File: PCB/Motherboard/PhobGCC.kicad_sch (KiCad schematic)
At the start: 57 parts, among them J1 Conn_01x06_Female, J2 Conn_01x04_Female, J3 Conn_01x01_Male, J5 Conn_01x02_Male, Q1 SSM3K56FS,LF, SW1 A, SW10 Dup, SW11 Dright, SW12 Ddown, SW2 B, SW3 X, SW4 Y, SW5 Start, SW6 L, SW7 R, SW8 1825027-5, SW9 Dleft, U1 Teensy4.0, U2 2x DRV5053CAQLPGM Hall Effect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, U3 BPR-105, U4 BPR-105

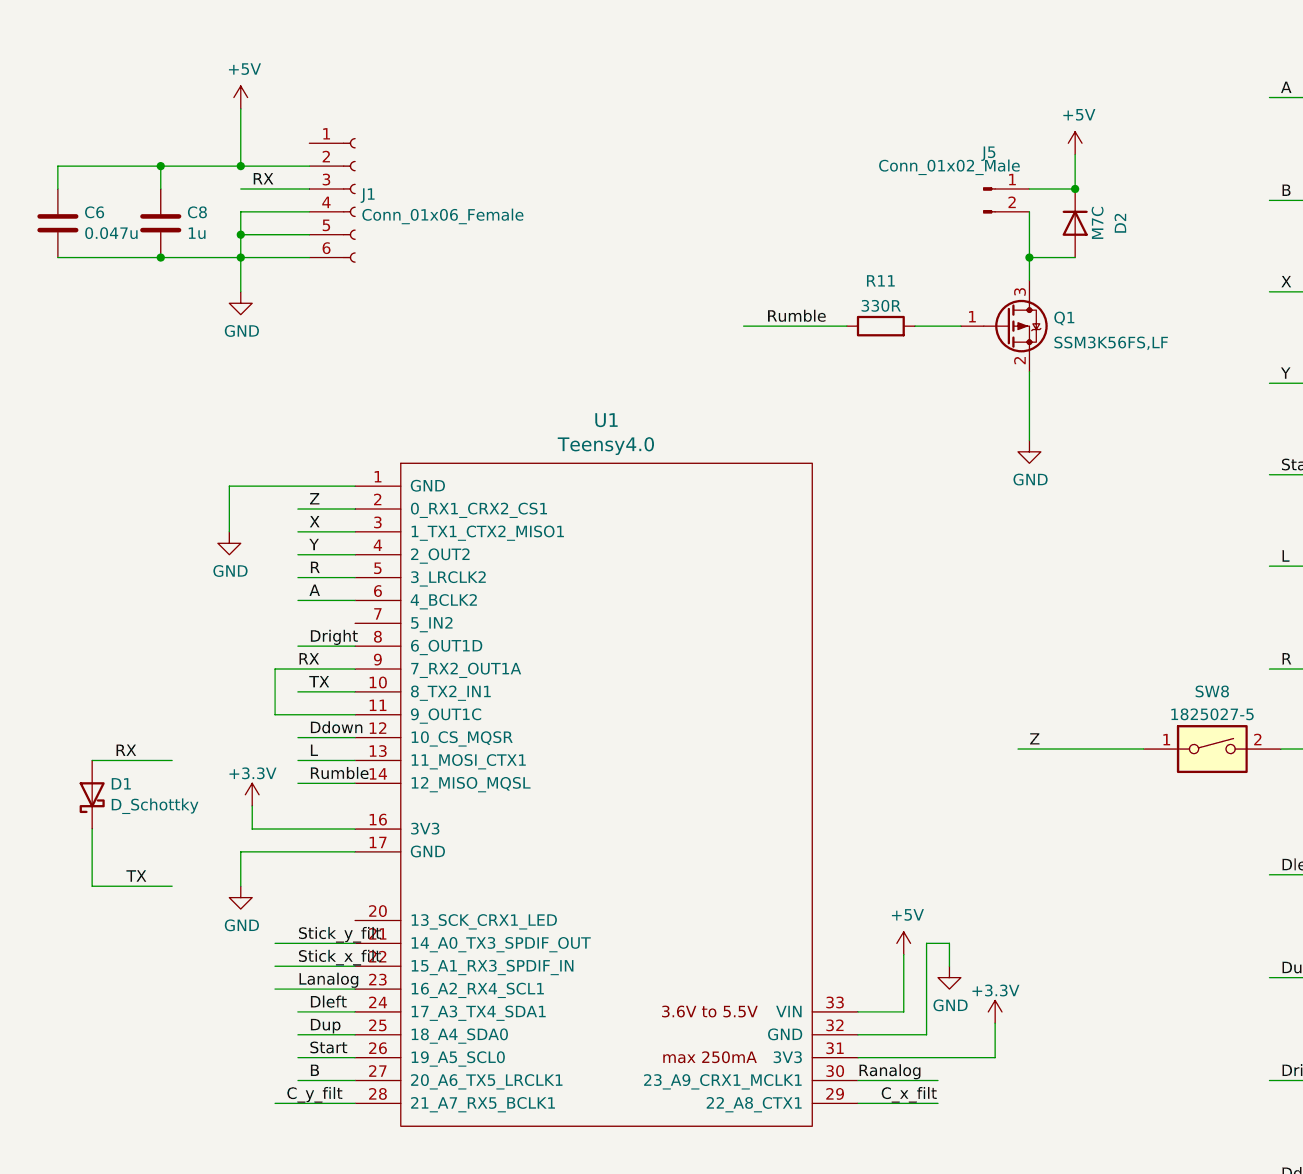
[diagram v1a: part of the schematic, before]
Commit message: Tidied up some things in the PCB, redid the ABXY contacts from an earlier file version, preview now works on jlcPCB
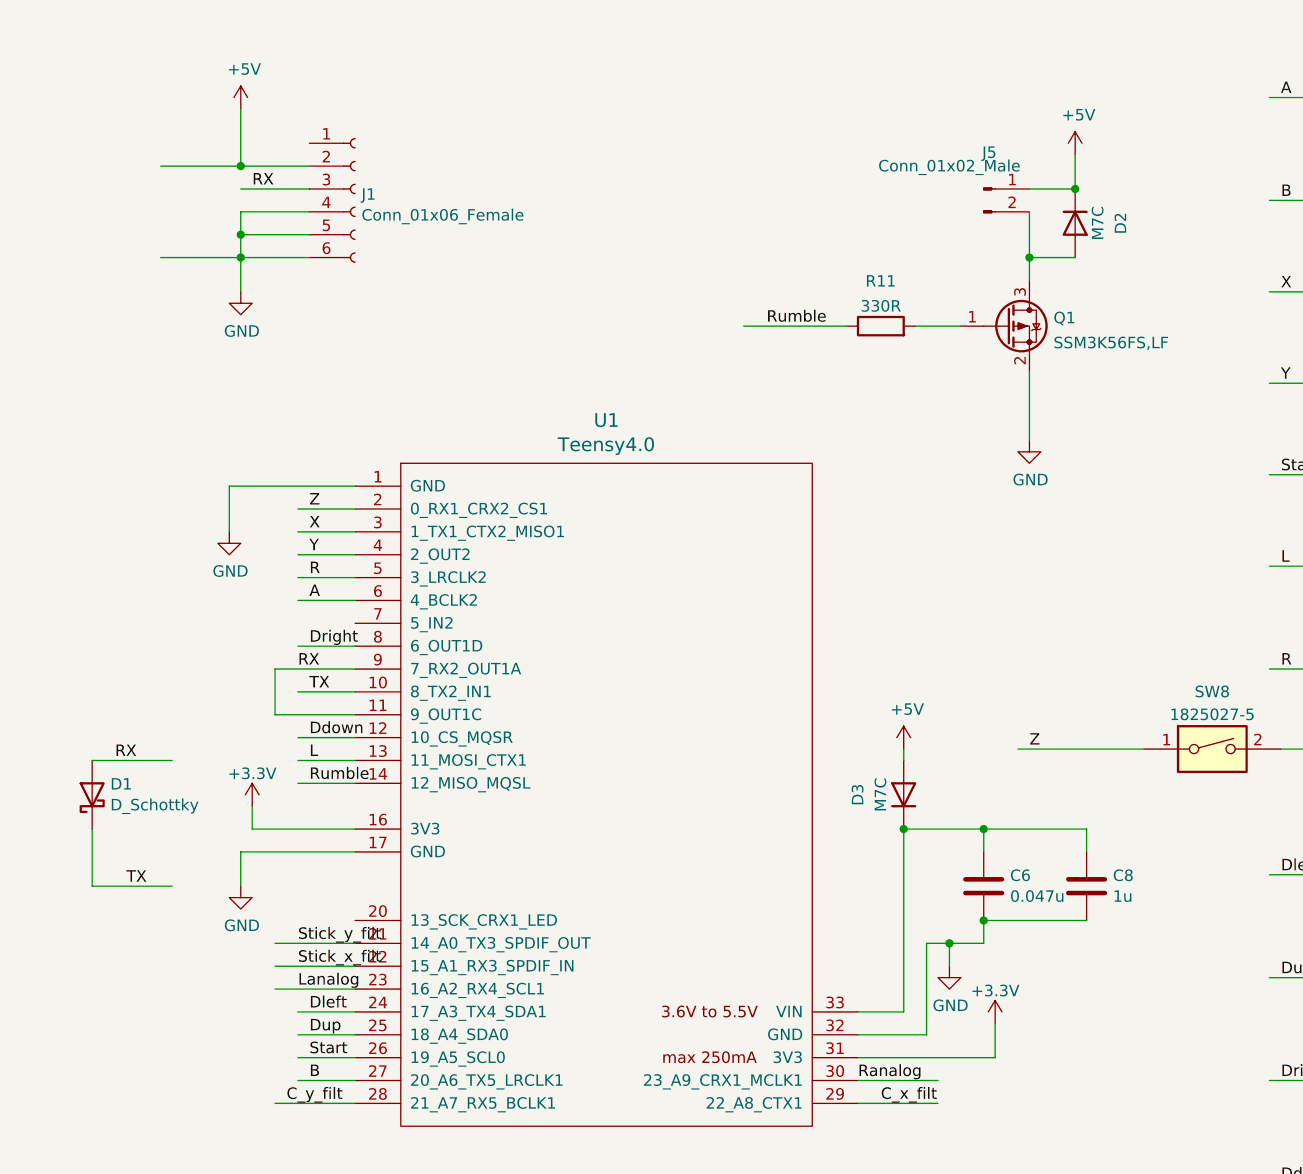
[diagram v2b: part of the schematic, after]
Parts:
- added D3: M7C, Diode_SMD:D_SOD-123F, symbol Device:D
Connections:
- net +5V: now also D3.2 (A); no longer C6.1, C8.1, U1.33 (VIN)
- new net: C6.1, C8.1, D3.1 (K), U1.33 (VIN)
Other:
- moved on the sheet: C6, C8
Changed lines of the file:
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@@
   (junction (at 133.35 180.34) (diameter 0) (color 0 0 0 0)
   )
+  (junction (at 119.38 116.84) (diameter 0) (color 0 0 0 0)
+  )
   (junction (at 177.8 44.45) (diameter 0) (color 0 0 0 0)
   )
@@
   (junction (at 177.8 132.08) (diameter 0) (color 0 0 0 0)
   )
+  (junction (at 123.19 104.14) (diameter 0) (color 0 0 0 0)
+  )
   (junction (at 90.17 180.34) (diameter 0) (color 0 0 0 0)
   )
@@
   (junction (at 80.01 180.34) (diameter 0) (color 0 0 0 0)
   )
+  (junction (at 114.3 104.14) (diameter 0) (color 0 0 0 0)
+  )
   (junction (at 228.6 31.75) (diameter 0) (color 0 0 0 0)
   )
@@
   (junction (at 76.2 168.91) (diameter 0) (color 0 0 0 0)
   )
-  (junction (at 31.75 40.64) (diameter 0) (color 0 0 0 0)
-  )
   (junction (at 99.06 180.34) (diameter 0) (color 0 0 0 0)
   )
@@
   (junction (at 40.64 40.64) (diameter 0) (color 0 0 0 0)
   )
+  (junction (at 123.19 114.3) (diameter 0) (color 0 0 0 0)
+  )
   (junction (at 226.06 59.69) (diameter 0) (color 0 0 0 0)
   )
@@
   (junction (at 76.2 180.34) (diameter 0) (color 0 0 0 0)
   )
-  (junction (at 31.75 30.48) (diameter 0) (color 0 0 0 0)
-  )
   (junction (at 209.55 143.51) (diameter 0) (color 0 0 0 0)
   )
@@
     (stroke (width 0) (type default) (color 0 0 0 0))
   )
+  (wire (pts (xy 123.19 114.3) (xy 123.19 116.84))
+    (stroke (width 0) (type default) (color 0 0 0 0))
+  )
   (wire (pts (xy 241.3 21.59) (xy 226.06 21.59))
     (stroke (width 0) (type default) (color 0 0 0 0))
   )
+  (wire (pts (xy 114.3 104.14) (xy 114.3 124.46))
+    (stroke (width 0) (type default) (color 0 0 0 0))
+  )
   (wire (pts (xy 40.64 180.34) (xy 60.96 180.34))
     (stroke (width 0) (type default) (color 0 0 0 0))
@@
     (stroke (width 0) (type default) (color 0 0 0 0))
   )
+  (wire (pts (xy 114.3 95.25) (xy 114.3 96.52))
+    (stroke (width 0) (type default) (color 0 0 0 0))
+  )
   (wire (pts (xy 53.34 86.36) (xy 44.45 86.36))
     (stroke (width 0) (type default) (color 0 0 0 0))
@@
     (stroke (width 0) (type default) (color 0 0 0 0))
   )
-  (wire (pts (xy 31.75 33.02) (xy 31.75 30.48))
-    (stroke (width 0) (type default) (color 0 0 0 0))
-  )
-  (wire (pts (xy 20.32 30.48) (xy 31.75 30.48))
+  (wire (pts (xy 134.62 106.68) (xy 134.62 104.14))
+    (stroke (width 0) (type default) (color 0 0 0 0))
+  )
+  (wire (pts (xy 114.3 104.14) (xy 123.19 104.14))
+    (stroke (width 0) (type default) (color 0 0 0 0))
+  )
+  (wire (pts (xy 123.19 104.14) (xy 134.62 104.14))
     (stroke (width 0) (type default) (color 0 0 0 0))
   )
@@
     (stroke (width 0) (type default) (color 0 0 0 0))
   )
-  (wire (pts (xy 20.32 30.48) (xy 20.32 33.02))
+  (wire (pts (xy 123.19 104.14) (xy 123.19 106.68))
     (stroke (width 0) (type default) (color 0 0 0 0))
   )
@@
     (stroke (width 0) (type default) (color 0 0 0 0))
   )
+  (wire (pts (xy 123.19 116.84) (xy 119.38 116.84))
+    (stroke (width 0) (type default) (color 0 0 0 0))
+  )
   (wire (pts (xy 163.83 74.93) (xy 154.94 74.93))
     (stroke (width 0) (type default) (color 0 0 0 0))
@@
     (stroke (width 0) (type default) (color 0 0 0 0))
   )
-  (wire (pts (xy 114.3 124.46) (xy 114.3 118.11))
-    (stroke (width 0) (type default) (color 0 0 0 0))
-  )
   (wire (pts (xy 173.99 143.51) (xy 177.8 143.51))
     (stroke (width 0) (type default) (color 0 0 0 0))
@@
     (stroke (width 0) (type default) (color 0 0 0 0))
   )
-  (wire (pts (xy 20.32 40.64) (xy 31.75 40.64))
+  (wire (pts (xy 123.19 114.3) (xy 134.62 114.3))
     (stroke (width 0) (type default) (color 0 0 0 0))
   )
@@
     (pin "1")
   )
-  (symbol (lib_id "Device:C") (at 31.75 36.83 0) (unit 1)
-    (in_bom yes) (on_board yes)
-    (property "Reference" "C8" (id 0) (at 34.671 35.6616 0)
-      (effects (font (size 1.27 1.27)) (justify left))
-    )
-    (property "Value" "1u" (id 1) (at 34.671 37.973 0)
-      (effects (font (size 1.27 1.27)) (justify left))
-    )
-    (property "Footprint" "Capacitors_SMD:C_0603_HandSoldering" (id 2) (at 32.7152 40.64 0)
-      (effects (font (size 1.27 1.27)) hide)
-    )
-    (property "Datasheet" "~" (id 3) (at 31.75 36.83 0)
-      (effects (font (size 1.27 1.27)) hide)
-    )
-    (property "LCSC" "C15849" (id 4) (at 31.75 36.83 0)
-      (effects (font (size 1.27 1.27)) hide)
-    )
-    (property "MPN" "CL10A105KB8NNNC" (id 5) (at 31.75 36.83 0)
-      (effects (font (size 1.27 1.27)) hide)
-    )
-    (property "Manufacturer" "Samsung Electro-Mechanics" (id 6) (at 31.75 36.83 0)
-      (effects (font (size 1.27 1.27)) hide)
-    )
-    (pin "1")
-    (pin "2")
-  )
-  (symbol (lib_id "power:+5V") (at 114.3 118.11 0) (unit 1)
-    (in_bom yes) (on_board yes)
-    (property "Reference" "#PWR0118" (id 0) (at 114.3 121.92 0)
-      (effects (font (size 1.27 1.27)) hide)
-    )
-    (property "Value" "+5V" (id 1) (at 114.681 113.7158 0))
-    (property "Footprint" "" (id 2) (at 114.3 118.11 0)
-      (effects (font (size 1.27 1.27)) hide)
-    )
-    (property "Datasheet" "" (id 3) (at 114.3 118.11 0)
+  (symbol (lib_id "Device:C") (at 134.62 110.49 0) (unit 1)
+    (in_bom yes) (on_board yes)
+    (property "Reference" "C8" (id 0) (at 137.541 109.3216 0)
+      (effects (font (size 1.27 1.27)) (justify left))
+    )
+    (property "Value" "1u" (id 1) (at 137.541 111.633 0)
+      (effects (font (size 1.27 1.27)) (justify left))
+    )
+    (property "Footprint" "Capacitors_SMD:C_0603_HandSoldering" (id 2) (at 135.5852 114.3 0)
+      (effects (font (size 1.27 1.27)) hide)
+    )
+    (property "Datasheet" "~" (id 3) (at 134.62 110.49 0)
+      (effects (font (size 1.27 1.27)) hide)
+    )
+    (property "LCSC" "C15849" (id 4) (at 134.62 110.49 0)
+      (effects (font (size 1.27 1.27)) hide)
+    )
+    (property "MPN" "CL10A105KB8NNNC" (id 5) (at 134.62 110.49 0)
+      (effects (font (size 1.27 1.27)) hide)
+    )
+    (property "Manufacturer" "Samsung Electro-Mechanics" (id 6) (at 134.62 110.49 0)
+      (effects (font (size 1.27 1.27)) hide)
+    )
+    (pin "1")
+    (pin "2")
+  )
+  (symbol (lib_id "power:+5V") (at 114.3 95.25 0) (unit 1)
+    (in_bom yes) (on_board yes)
+    (property "Reference" "#PWR0118" (id 0) (at 114.3 99.06 0)
+      (effects (font (size 1.27 1.27)) hide)
+    )
+    (property "Value" "+5V" (id 1) (at 114.681 90.8558 0))
+    (property "Footprint" "" (id 2) (at 114.3 95.25 0)
+      (effects (font (size 1.27 1.27)) hide)
+    )
+    (property "Datasheet" "" (id 3) (at 114.3 95.25 0)
       (effects (font (size 1.27 1.27)) hide)
     )
@@
     (pin "2")
   )
+  (symbol (lib_id "Device:D") (at 114.3 100.33 90) (unit 1)
+    (in_bom yes) (on_board yes)
+    (property "Reference" "D3" (id 0) (at 109.22 100.33 0))
+    (property "Value" "M7C" (id 1) (at 111.76 100.33 0))
+    (property "Footprint" "Diode_SMD:D_SOD-123F" (id 2) (at 114.3 100.33 0)
+      (effects (font (size 1.27 1.27)) hide)
+    )
+    (property "Datasheet" "~" (id 3) (at 114.3 100.33 0)
+      (effects (font (size 1.27 1.27)) hide)
+    )
+    (property "JLCPN" "C95872" (id 4) (at 114.3 100.33 0)
+      (effects (font (size 1.27 1.27)) hide)
+    )
+    (pin "1")
+    (pin "2")
+  )
   (symbol (lib_id "Sensor_Proximity:BPR-105") (at 201.93 146.05 0) (unit 1)
     (in_bom yes) (on_board yes) (fields_autoplaced)
@@
     (pin "1")
   )
-  (symbol (lib_id "Device:C") (at 20.32 36.83 0) (unit 1)
-    (in_bom yes) (on_board yes)
-    (property "Reference" "C6" (id 0) (at 23.241 35.6616 0)
-      (effects (font (size 1.27 1.27)) (justify left))
-    )
-    (property "Value" "0.047u" (id 1) (at 23.241 37.973 0)
-      (effects (font (size 1.27 1.27)) (justify left))
-    )
-    (property "Footprint" "Capacitors_SMD:C_0603_HandSoldering" (id 2) (at 21.2852 40.64 0)
-      (effects (font (size 1.27 1.27)) hide)
-    )
-    (property "Datasheet" "~" (id 3) (at 20.32 36.83 0)
-      (effects (font (size 1.27 1.27)) hide)
-    )
-    (property "LCSC" "C1604" (id 4) (at 20.32 36.83 0)
-      (effects (font (size 1.27 1.27)) hide)
-    )
-    (property "MPN" "0603B222K500NT" (id 5) (at 20.32 36.83 0)
-      (effects (font (size 1.27 1.27)) hide)
-    )
-    (property "Manufacturer" "FH(Guangdong Fenghua Advanced Tech)" (id 6) (at 20.32 36.83 0)
+  (symbol (lib_id "Device:C") (at 123.19 110.49 0) (unit 1)
+    (in_bom yes) (on_board yes)
+    (property "Reference" "C6" (id 0) (at 126.111 109.3216 0)
+      (effects (font (size 1.27 1.27)) (justify left))
+    )
+    (property "Value" "0.047u" (id 1) (at 126.111 111.633 0)
+      (effects (font (size 1.27 1.27)) (justify left))
+    )
+    (property "Footprint" "Capacitors_SMD:C_0603_HandSoldering" (id 2) (at 124.1552 114.3 0)
+      (effects (font (size 1.27 1.27)) hide)
+    )
+    (property "Datasheet" "~" (id 3) (at 123.19 110.49 0)
+      (effects (font (size 1.27 1.27)) hide)
+    )
+    (property "LCSC" "C1604" (id 4) (at 123.19 110.49 0)
+      (effects (font (size 1.27 1.27)) hide)
+    )
+    (property "MPN" "0603B222K500NT" (id 5) (at 123.19 110.49 0)
+      (effects (font (size 1.27 1.27)) hide)
+    )
+    (property "Manufacturer" "FH(Guangdong Fenghua Advanced Tech)" (id 6) (at 123.19 110.49 0)
       (effects (font (size 1.27 1.27)) hide)
     )
@@
       (reference "D2") (unit 1) (value "M7C") (footprint "Diode_SMD:D_SOD-123F")
     )
+    (path "/c45ca1ab-50a8-4158-9b8e-86eb478b26b1"
+      (reference "D3") (unit 1) (value "M7C") (footprint "Diode_SMD:D_SOD-123F")
+    )
     (path "/00000000-0000-0000-0000-000061ce47a0"

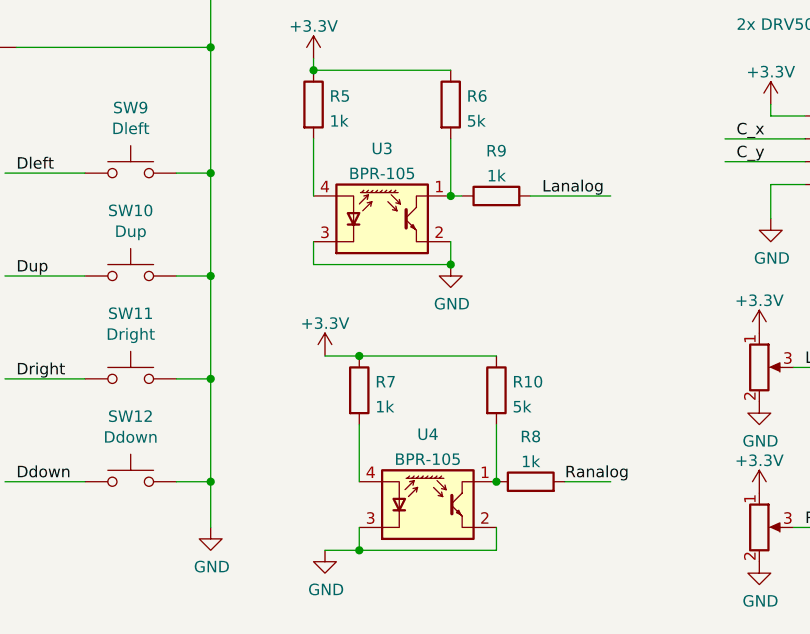
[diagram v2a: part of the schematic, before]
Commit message: More cleanup and teaking of the PCBs, made BOM and placement files for JLC
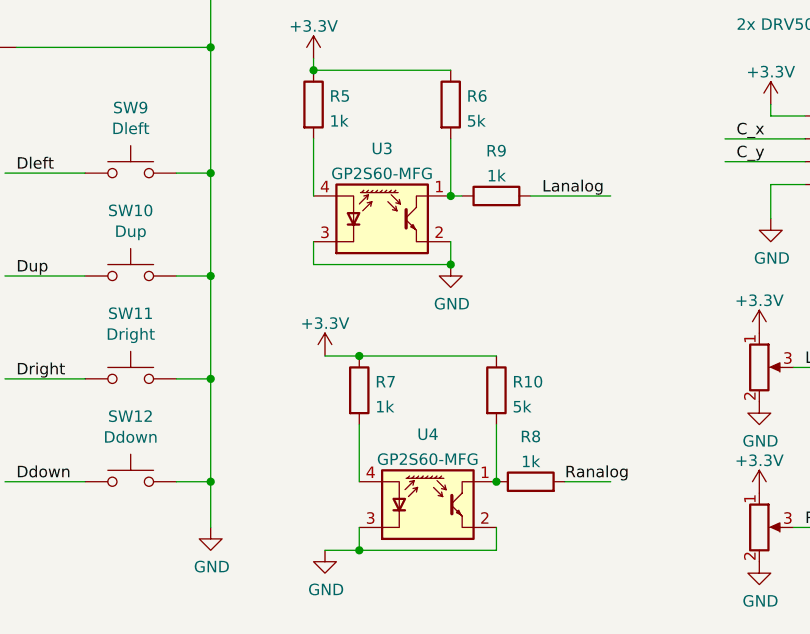
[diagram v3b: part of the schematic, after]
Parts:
- C10, C11, C12, C8: footprint Capacitors_SMD:C_0603_HandSoldering -> Capacitor_SMD:C_0603_1608Metric_Pad1.08x0.95mm_HandSolder
- D1: LCSC C151333 -> C8524; MPN SDM03U40-7 -> RB751S-40; Manufacturer Diodes Incorporated -> Changjiang Electronics Tech (CJ); Manufacturer PN SDM03U40-7 -> RB751S-40
- D2, D3: JLCPN C95872 -> (none); LCSC (none) -> C95872; MPN (none) -> M7; Manufacturer (none) -> MDD (Microdiode Electronics)
- Q1: footprint Package_TO_SOT_SMD:SOT-416 -> Package_TO_SOT_SMD:SOT-23; LCSC (none) -> C8545; MPN (none) -> 2N7002; Manufacturer (none) -> Changjiang Electronics Tech (CJ)
- R10, R6: LCSC (none) -> C23162; MPN (none) -> 0603WAF4701T5E; Manufacturer (none) -> UNI-ROYAL(Uniroyal Elec)
- R11: LCSC (none) -> C23138; MPN (none) -> 0603WAF3300T5E; Manufacturer (none) -> UNI-ROYAL(Uniroyal Elec)
- R5, R7, R8, R9: LCSC (none) -> C25804; MPN (none) -> 0603WAF1002T5E; Manufacturer (none) -> UNI-ROYAL
- SW1, SW2, SW3, SW4: footprint Gamecube MB:ABXY_layout_small_mask_omron_switch2 -> Gamecube MB:ABXY_Contact_Omron_Switch
- U3, U4: value BPR-105 -> GP2S60-MFG
